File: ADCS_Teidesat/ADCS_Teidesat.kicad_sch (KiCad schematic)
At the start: 38 parts, among them IC1 BHI385, IC2 L86-M33, IC3 MAX2659ELT+T, IC4 THVD1400DR, IC5 TMS5703137DZWTQQ1, U1 LIS2DS12TR, Y1 ATX-H13-F-16.000MHz-G100-T

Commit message: Desarrollo Antena, filtros y oscilador
Circuito del oscilador, la antena GNSS y sus respectivos filtro

Co-Authored-By: hugohdezmo <238262256+hugohdezmo@users.noreply.github.com>
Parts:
- removed IC5: TMS5703137DZWTQQ1, BGA337C80P19X19_1600X1600X140, symbol TMS5703137DZWTQQ1:TMS5703137DZWTQQ1
- added C10: 100n, symbol Device:C
- added C11: F6QA1G581M2QZ-J, Huellas ADCS:F6QA1G581M2QZJ, symbol F6QA1G581M2QZ-J:F6QA1G581M2QZ-J
- added IC5: TMS5703137DPGEQQ1, Huellas ADCS:QFP50P2200X2200X160-144N, symbol TMS5703137DPGEQQ1:TMS5703137DPGEQQ1
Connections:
- net +3V3: now also IC3.4 (VCC), IC3.5 (~{SHDN}), Y1.1 (~{INH}), Y1.4 (VDD), C10.1
- net GND: now also AE1.4 (RETURN/GND), IC3.1 (GND_1), IC3.2 (GND_2), C10.2, C11.2 (GND_1), C11.3 (GND_2), C11.5 (GND_3)
- net RF: now reaches IC3.3 (RFIN)
- net RF: now also C11.4 (OUT)
- net OUT ANT: now reaches IC3.6 (RFOUT)
- net OUT ANT: now also IC2.13 (RF_IN)
- net ANTENNA: now reaches AE1.3 (FEED)
- net ANTENNA: now also C11.1 (IN)
- net OUT OSC: now reaches Y1.3 (OUTPUT)
- net OUT OSC: now also IC5.18 (OSCIN)
- net Sensor Solar1 renamed SUN SENSOR1
- net Sensor Solar2 renamed SUN SENSOR2
- net Sensor Solar3 renamed SUN SENSOR3
- net Sensor Solar4 renamed SUN SENSOR4
- net Sensor Solar5 renamed SUN SENSOR5
- no-connect marks 8 -> 9
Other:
- note added: "Antena"
- note added: "Filtro RF"
- note added: "Filtros"
- note added: "OSCILADOR"
- note added: "Pin añadido por nosotros preguntar a Salvador"
- company: (none) -> Teidesat
- title: (none) -> Placa ADCS del nanosatélite Teidesat
- moved on the sheet: AE1, C5, C6, C7, C8, C9, D1, D2, D3, D4, D5, IC1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

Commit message: Conexión del GNSS
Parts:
- removed C6, C7, C8, C9: C, symbol Device:C
- removed D1, D2, D3, D4, D5: VBP104SR, Huellas ADCS:SOD6439X130N, symbol VBP104SR:VBP104SR
- removed R10, R2, R4, R6, R8: 1K, symbol Device:R
- removed R3, R5, R7, R9: 47K, symbol Device:R
- C5: value C -> 100n
- R1: value 47K -> 10k
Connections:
- net SUN SENSOR1 is gone; now on net +3V3: C5.1
- net +3V3: now also IC2.11 (EX_ANT), IC2.4 (VCC), IC2.5 (V_BCKP), IC2.7 (FORCE_ON), R1.1
- net GND: now also IC2.10 (RESET), IC2.12 (GND_2), IC2.3 (GND_1)
- net data in: now reaches IC2.1 (RXD1)
- net data in: now also IC5.6 (N2HET1[11])
- net data out: now reaches IC2.2 (TXD1)
- net data out: now also IC5.39 (N2HET1[13])
- net 1PPS: now reaches IC2.6 (1PPS)
- net 1PPS: now also IC5.25 (N2HET1[0])
- no-connect marks 9 -> 10
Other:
- note added: "A N2HET1[0] del micro"
- note added: "El pin 5 podría ir conectado a una pila o un supercapacitor para poder hacer un hot start"
- note added: "Los pines 1 y 2 van conectados al pin de transmisión y al pin de recepción del micro respectivamente. N2HET1[11]-----N2HET1[13]"
- note removed: "Fotodiodo"
- note removed: "Pin añadido por nosotros preguntar a Salvador"
- note removed: "Polarización inversa"
- note removed: "Sensores Solares"
- moved on the sheet: IC1, IC2, IC4, U1

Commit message: Conexión de IMU con el Microcontrolador
Conexión de la IMU (LSM6DSV16XTR) y del magnetómetro (LIS2MDLTR). Se han conectado de las forma que trabajen en modo SPI
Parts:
- removed IC1: BHI385, Huellas ADCS:BHI385, symbol BHI385:BHI385
- added C6, C7, C9: 100n, symbol Device:C
- added C8: 220n, symbol Device:C
- added IC6: BHI385, Huellas ADCS:BHI385, symbol BHI385:BHI385
- added IC7: LSM6DSV16XTR, LSM6DSV16BXTR, symbol LSM6DSV16XTR:LSM6DSV16XTR
- added IC8: LIS2MDLTR, LGA-12, symbol LIS2MDLTR:LIS2MDLTR
- added R2: 10k, symbol Device:R
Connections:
- net +3V3: now also C6.1, C7.1, C9.1, IC7.10 (OCS_AUX), IC7.5 (VDD_IO), IC7.8 (VDD), IC8.10 (VDD_IO), IC8.9 (VDD), R2.1
- net GND: now also C6.2, C7.2, C8.1, C9.2, IC6.7 (GND), IC7.1 (SDO/SA0), IC7.11 (SDO_AUX), IC7.2 (SDX/AH1/QVAR1), IC7.3 (SCX/AH2/QVAR2), IC7.6 (GND_1), IC7.7 (GND_2), IC8.6 (GND_1), IC8.8 (GND_2), R2.2
- net INT 2: now reaches IC5.14 (GIOA[5])
- net INT 2: now also IC7.9 (INT2)
- net CS IMU: now reaches IC5.16 (GIOA[6])
- net CS IMU: now also IC7.12 (CS)
- net CS MAGNETÓMETRO: now reaches IC5.22 (GIOA[7])
- net CS MAGNETÓMETRO: now also IC8.3 (CS)
- net INT MAGNETÓMETRO: now reaches IC5.55 (MIBSPI3NCS[0])
- net INT MAGNETÓMETRO: now also IC8.7 (INT/DRDY)
- net INT 1: now reaches IC5.9 (GIOA[2])
- net INT 1: now also IC7.4 (INT1)
- net IMU/MAGNETÓMETRO: now reaches IC5.94 (MIBSPI1SOMI)
- net IMU/MAGNETÓMETRO: now also IC7.14 (SDA), IC8.4 (SDA/SDI/SDO)
- net SCL/SPC MAG.: now reaches IC5.95 (MIBSPI1CLK)
- net SCL/SPC MAG.: now also IC8.1 (SCL/SPC)
- new net: C8.2, IC8.5 (C1)
- new net INTERRUPCIÓN 1: IC6.4 (HIRQ)
- new net MAGNETÓMETRO: IC6.2 (ASDX)
- no-connect marks 10 -> 16
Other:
- note added: "IMU+MAGNETÓMETRO-DESCARTADOS"
- note added: "MAGNETÓMETRO"
- moved on the sheet: U1

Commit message: Arreglos etiquetas
Correcciones propuestas por salvador acerca de etiquetas
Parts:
- removed IC6: BHI385, Huellas ADCS:BHI385, symbol BHI385:BHI385
- removed U1: LIS2DS12TR, Huellas ADCS:LGA12R50P4X4_200X200X86, symbol LIS2DS12TR:LIS2DS12TR
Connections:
- net +3V3: no longer H2.27 (Pin_27), H2.28 (Pin_28)
- net GND: no longer H2.21 (Pin_21), H2.22 (Pin_22), H2.29 (Pin_29), H2.30 (Pin_30), H2.31 (Pin_31), H2.32 (Pin_32)
- net INT 1: no longer IC5.9 (GIOA[2])
- net INT 2: no longer IC5.14 (GIOA[5])
- net +5V: no longer names the net of H2.25 (Pin_25)
- net +5V: no longer H2.26 (Pin_26)
- net +BATT: no longer names the net of H2.45 (Pin_45)
- net +BATT: no longer H2.46 (Pin_46)
- net 5VIN: no longer names the net of H1.32 (Pin_32)
- removed net BCR_OUT: H2.41 (Pin_41), H2.42 (Pin_42), H2.43 (Pin_43), H2.44 (Pin_44)
- net CRX3/GP30: no longer names the net of H1.29 (Pin_29)
- net CS IMU renamed CS_IMU
- net CS MAGNETÓMETRO renamed CS_MAGNETÓMETRO
- net CS/GP10: no longer names the net of H1.46 (Pin_46)
- net CS/GP36: no longer names the net of H1.50 (Pin_50)
- net CS/GP37: no longer names the net of H1.48 (Pin_48)
- net CTX3/GP31: no longer names the net of H1.31 (Pin_31)
- net GP14/A0/TX3: no longer names the net of H1.15 (Pin_15)
- net GP15/A1/RX3: no longer names the net of H1.13 (Pin_13)
- net GP2: no longer names the net of H1.4 (Pin_4)
- net GP20/A6/TX5: no longer names the net of H1.19 (Pin_19)
- net GP21/A7/RX5: no longer names the net of H1.17 (Pin_17)
- net GP22/A8: no longer names the net of H1.18 (Pin_18)
- net GP23/A9: no longer names the net of H1.16 (Pin_16)
- net GP3: no longer names the net of H1.6 (Pin_6)
- net GP32: no longer names the net of H1.28 (Pin_28)
- net GP33: no longer names the net of H1.30 (Pin_30)
- net GP38/A14: no longer names the net of H1.26 (Pin_26)
- net GP39/A15: no longer names the net of H1.24 (Pin_24)
- net GP4: no longer names the net of H1.8 (Pin_8)
- net GP40/A16: no longer names the net of H1.22 (Pin_22)
- net GP41/A17: no longer names the net of H1.20 (Pin_20)
- net GP5: no longer names the net of H1.10 (Pin_10)
- net GP6: no longer names the net of H1.12 (Pin_12)
- net GP9: no longer names the net of H1.14 (Pin_14)
- net INT MAGNETÓMETRO renamed INT_MAGNETÓMETRO
- net MISO0: no longer names the net of H1.38 (Pin_38)
- net MISO1: no longer names the net of H1.44 (Pin_44)
- net MOSI0: no longer names the net of H1.36 (Pin_36)
- net MOSI1: no longer names the net of H1.42 (Pin_42)
- net OUT ANT renamed OUT_ANT
- net OUT OSC renamed OUT_OSC
- net PCM_IN: no longer names the net of H2.35 (Pin_35)
- net PCM_IN: no longer H2.36 (Pin_36)
- net RX1/GP0: no longer names the net of H1.5 (Pin_5)
- net RX2/GP7: no longer names the net of H1.9 (Pin_9)
- net RX7/GP28: no longer names the net of H1.21 (Pin_21)
- net RX8/GP34: no longer names the net of H1.25 (Pin_25)
- net SCK0: no longer names the net of H1.34 (Pin_34)
- net SCK1: no longer names the net of H1.40 (Pin_40)
- net SCL0: no longer names the net of H1.43 (Pin_43)
- net SCL1: no longer names the net of H1.39 (Pin_39)
- net SCL2: no longer names the net of H1.35 (Pin_35)
- net SCL/SPC MAG. renamed SPC_MAG.
- net SDA0: no longer names the net of H1.41 (Pin_41)
- net SDA1: no longer names the net of H1.37 (Pin_37)
- net SDA2: no longer names the net of H1.33 (Pin_33)
- net SW1: no longer names the net of H2.9 (Pin_9)
- net SW10: no longer names the net of H2.18 (Pin_18)
- net SW11: no longer names the net of H2.19 (Pin_19)
- net SW12: no longer names the net of H2.20 (Pin_20)
- net SW2: no longer names the net of H2.10 (Pin_10)
- net SW3: no longer names the net of H2.11 (Pin_11)
- net SW4: no longer names the net of H2.12 (Pin_12)
- net SW5: no longer names the net of H2.13 (Pin_13)
- net SW6: no longer names the net of H2.14 (Pin_14)
- net SW7: no longer names the net of H2.15 (Pin_15)
- net SW8: no longer names the net of H2.16 (Pin_16)
- net SW9: no longer names the net of H2.17 (Pin_17)
- net TX1/GP1: no longer names the net of H1.7 (Pin_7)
- net TX2/GP8: no longer names the net of H1.11 (Pin_11)
- net TX7/GP29: no longer names the net of H1.23 (Pin_23)
- net TX8/GP35: no longer names the net of H1.27 (Pin_27)
- net data in renamed DATA_IN
- net data out renamed DATA_OUT
- new net INT1: IC5.9 (GIOA[2])
- new net INT2: IC5.14 (GIOA[5])
- no-connect marks 16 -> 242
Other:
- note removed: "IMU+MAGNETÓMETRO-DESCARTADOS"
- note removed: "Magnetómetro"

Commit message: Comienzo PCB
Realizamos los últimos arreglos en las huellas de los componentes y comenzamos el diseño de la PCB

Co-Authored-By: hugohdezmo <238262256+hugohdezmo@users.noreply.github.com>
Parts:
- C10, C5, C6, C7, C8, C9: footprint (none) -> Capacitor_SMD:C_0805_2012Metric
- IC7: footprint LSM6DSV16BXTR -> Huellas ADCS:XDCR_LSM6DSV16XTR
- IC8: footprint LGA-12 -> Huellas ADCS:PQFN50P200X200X70-12N
- R1, R2: footprint (none) -> Resistor_SMD:R_0201_0603Metric
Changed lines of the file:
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@@
 			)
 		)
-		(property "Footprint" ""
+		(property "Footprint" "Resistor_SMD:R_0201_0603Metric"
 			(at 18.542 222.25 90)
 			(effects
@@
 			)
 		)
-		(property "Footprint" ""
+		(property "Footprint" "Capacitor_SMD:C_0805_2012Metric"
 			(at 51.7652 262.89 0)
 			(effects
@@
 			)
 		)
-		(property "Footprint" ""
+		(property "Footprint" "Resistor_SMD:R_0201_0603Metric"
 			(at 21.082 149.86 90)
 			(effects
@@
 			)
 		)
-		(property "Footprint" ""
+		(property "Footprint" "Capacitor_SMD:C_0805_2012Metric"
 			(at 97.4852 153.67 0)
 			(effects
@@
 			)
 		)
-		(property "Footprint" "LSM6DSV16BXTR"
+		(property "Footprint" "Huellas ADCS:XDCR_LSM6DSV16XTR"
 			(at 85.09 310.82 0)
 			(effects
@@
 			)
 		)
-		(property "Footprint" "LGA-12"
+		(property "Footprint" "Huellas ADCS:PQFN50P200X200X70-12N"
 			(at 189.23 328.6 0)
 			(effects
@@
 			)
 		)
-		(property "Footprint" ""
+		(property "Footprint" "Capacitor_SMD:C_0805_2012Metric"
 			(at 33.9852 38.1 0)
 			(effects
@@
 			)
 		)
-		(property "Footprint" ""
+		(property "Footprint" "Capacitor_SMD:C_0805_2012Metric"
 			(at 133.6548 245.11 0)
 			(effects
@@
 			)
 		)
-		(property "Footprint" ""
+		(property "Footprint" "Capacitor_SMD:C_0805_2012Metric"
 			(at 103.8352 241.3 0)
 			(effects
@@
 			)
 		)
-		(property "Footprint" ""
+		(property "Footprint" "Capacitor_SMD:C_0805_2012Metric"
 			(at 215.5952 251.46 0)
 			(effects

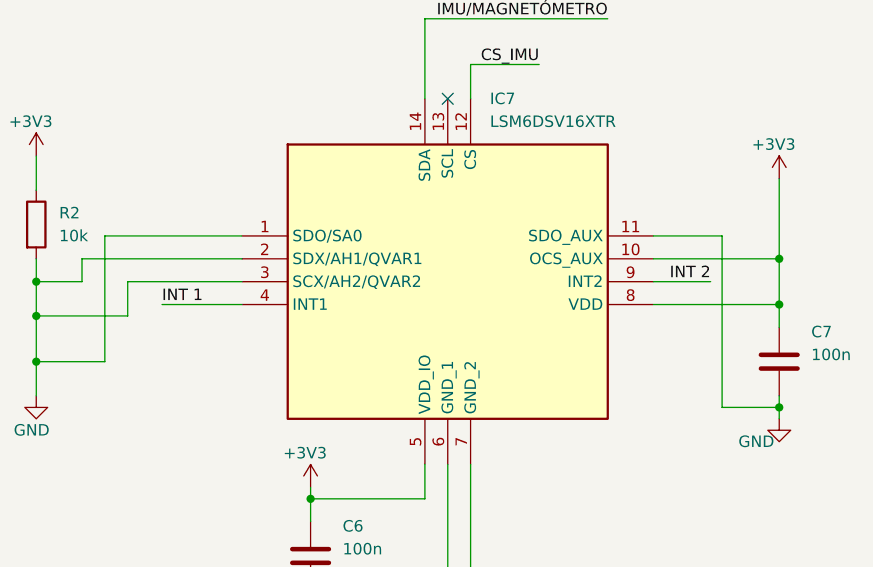
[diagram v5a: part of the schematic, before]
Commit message: Conexionado de componentes de PCB a falta de revisión
Se ha hecho un primer enrutado de la PCB de la placa ADCS.

Co-Authored-By: Angel-Castro-Vega <236372966+Angel-Castro-Vega@users.noreply.github.com>
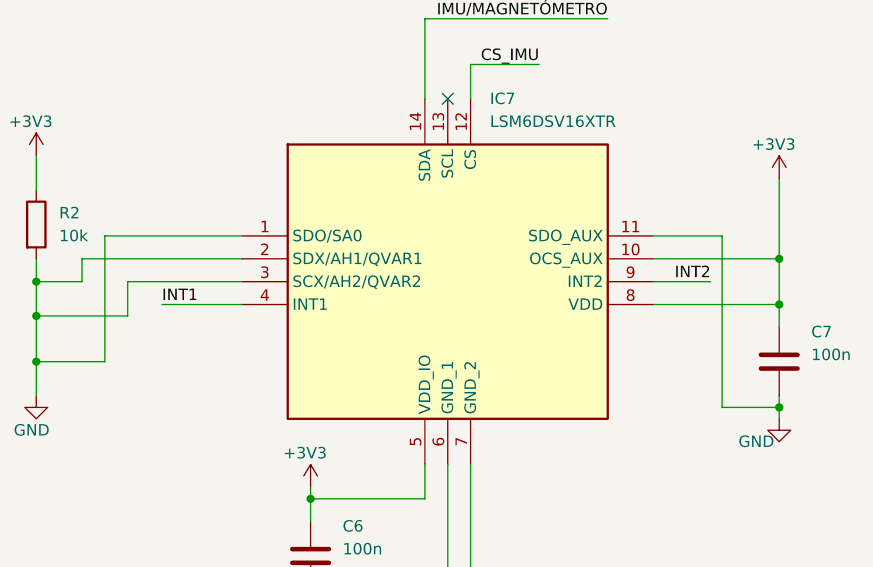
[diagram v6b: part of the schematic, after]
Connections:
- net INT 1 is gone; now on net INT1: IC7.4 (INT1)
- net INT 2 is gone; now on net INT2: IC7.9 (INT2)
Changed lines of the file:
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@@
 		)
 	)
-	(label "INT 2"
+	(label "INT2"
 		(at 95.25 228.6 180)
 		(effects
@@
 		)
 	)
-	(label "INT 1"
+	(label "INT1"
 		(at 34.29 231.14 0)
 		(effects

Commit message: Nuevo enrutado y correcciones de nombres y plantilla.
Co-Authored-By: Angel-Castro-Vega <236372966+Angel-Castro-Vega@users.noreply.github.com>
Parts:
- removed C8: 220n, Capacitor_SMD:C_0805_2012Metric, symbol Device:C
- removed C9: 100n, Capacitor_SMD:C_0805_2012Metric, symbol Device:C
- removed IC4: THVD1400DR, Huellas ADCS:SOIC127P600X175-8N, symbol THVD1400DR:THVD1400DR
- removed R2: 10k, Resistor_SMD:R_0201_0603Metric, symbol Device:R
- added C3, C5: 100n, Capacitor_SMD:C_0805_2012Metric, symbol Device:C
- added R1: 10k, Resistor_SMD:R_0201_0603Metric, symbol Device:R
- added R3: 33, Resistor_SMD:R_0201_0603Metric, symbol Device:R
- C6: value 100n -> 220n
- renumbered C11 to C1, C3 to C10, C4 to C11, C10 to C2, C5 to C4, C1 to C8, C2 to C9, R1 to R2, IC3 to U1, IC2 to U2, IC7 to U3, IC8 to U4, IC5 to U5
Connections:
- net +3V3: now also C3.1, C5.1, R1.1; no longer C6.1
- net GND: now also C6.1, C3.2, C5.2, R1.2; no longer C6.2
- net CLOCK_IMU: now reaches U3.13 (SCL)
- net CLOCK_IMU: now also U5.100 (MIBSPI5CLK)
- net at U5.106 (N2HET1[08]): now also R3.1
- net at U4.5 (C1): now also C6.2
- net IMU/MAGNETÓMETRO renamed MAGNETÓMETRO
- net MAGNETÓMETRO: no longer U3.14 (SDA)
- new net SIMO_IMU: R3.2, U3.14 (SDA)
- no-connect marks 242 -> 239
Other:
- note removed: "Interfaz digital hacia OBC"
- moved on the sheet: AE1, C1, C10, C11, C2, C4, C8, C9, H1, H2, MH1, MH2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
